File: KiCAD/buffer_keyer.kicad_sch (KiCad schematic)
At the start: 87 parts, among them J1 Conn_01x02_Pin, J13 Conn_01x05, J16 Conn_01x05, T1 2N3906, T2 2N3906, U15 LM7805_TO220, U19 L79L08_TO92, U20 ICL7660S, U3 MC1496, U4 MCP4921, U6 LM7171xIN, U7 LM7171xIN, U8 MCP4728

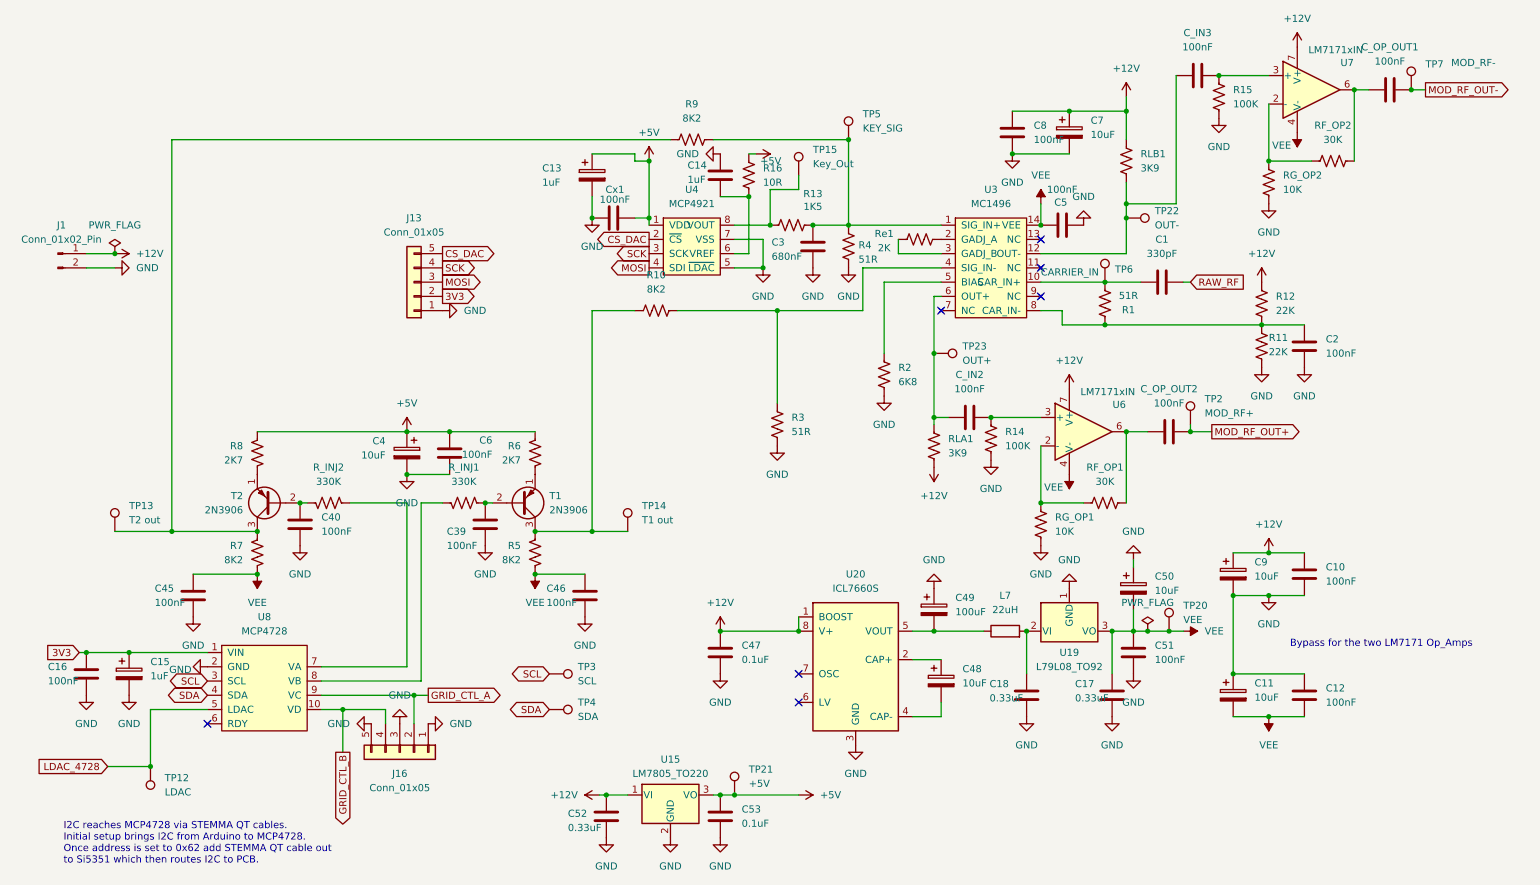
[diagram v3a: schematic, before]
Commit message: kicad: label critical anon nets on buffer_keyer for netclass matching
Global labels on MC1496 out (MC_OUT+/-), LM7171 driver outputs
(DRV_OUT+/-), T1/T2 collectors, and MCP4728 injection nodes
(VA_INJ/VB_INJ). Referenced by RF and HIZ patterns in netclass_patterns.

Co-Authored-By: Claude Opus 4.7 <noreply@anthropic.com>
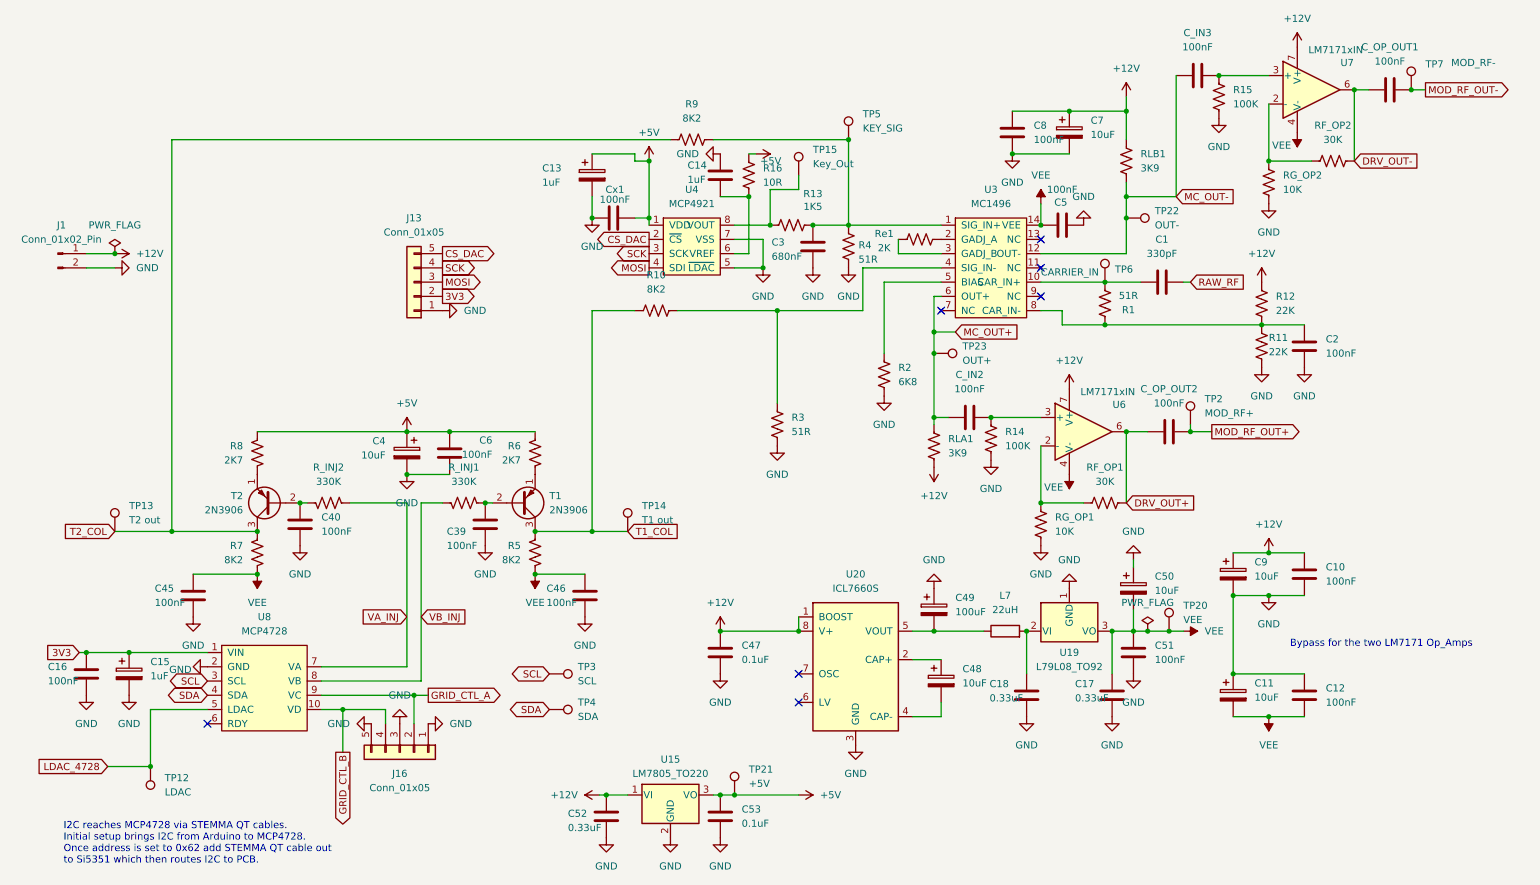
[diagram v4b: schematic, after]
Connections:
- net MC_OUT+: now reaches C_IN2.1, RLA1.2, TP23.1, U3.6 (OUT+)
- net T1_COL: now reaches R10.1, R5.1, T1.3 (C), TP14.1
- net MC_OUT-: now reaches C_IN3.1, RLB1.2, TP22.1, U3.12 (OUT-)
- net T2_COL: now reaches R7.1, R9.1, T2.3 (C), TP13.1
- net VA_INJ: now reaches R_INJ2.1, U8.7 (VA)
- net DRV_OUT-: now reaches C_OP_OUT1.1, RF_OP2.2, U7.6
- net VB_INJ: now reaches R_INJ1.2, U8.8 (VB)
- net DRV_OUT+: now reaches C_OP_OUT2.1, RF_OP1.2, U6.6
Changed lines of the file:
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@@
-	)
-	(junction
-		(at 212.09 52.07)
-		(diameter 0)
-		(color 0 0 0 0)
 	)
 	(junction
@@
 	)
 	(junction
+		(at 177.8 74.93)
+		(diameter 0)
+		(color 0 0 0 0)
+	)
+	(junction
 		(at 237.49 44.45)
 		(diameter 0)
@@
 	(junction
 		(at 142.24 157.48)
+		(diameter 0)
+		(color 0 0 0 0)
+	)
+	(junction
+		(at 212.09 50.8)
 		(diameter 0)
 		(color 0 0 0 0)
@@
 	(wire
 		(pts
-			(xy 212.09 54.61) (xy 212.09 52.07)
+			(xy 212.09 50.8) (xy 212.09 54.61)
 		)
 		(stroke
@@
 	(wire
 		(pts
+			(xy 212.09 50.8) (xy 212.09 48.26)
+		)
+		(stroke
+			(width 0)
+			(type default)
+		)
+	)
+	(wire
+		(pts
 			(xy 177.8 78.74) (xy 177.8 90.17)
 		)
@@
 	(wire
 		(pts
-			(xy 212.09 52.07) (xy 220.98 52.07)
+			(xy 212.09 50.8) (xy 220.98 50.8)
 		)
 		(stroke
@@
 	(wire
 		(pts
+			(xy 181.61 74.93) (xy 177.8 74.93)
+		)
+		(stroke
+			(width 0)
+			(type default)
+		)
+	)
+	(wire
+		(pts
 			(xy 87.63 139.7) (xy 85.09 139.7)
 		)
@@
 	(wire
 		(pts
-			(xy 220.98 52.07) (xy 220.98 29.21)
-		)
-		(stroke
-			(width 0)
-			(type default)
-		)
-	)
-	(wire
-		(pts
-			(xy 212.09 52.07) (xy 212.09 48.26)
+			(xy 220.98 50.8) (xy 220.98 29.21)
 		)
 		(stroke
@@
 	(wire
 		(pts
+			(xy 177.8 74.93) (xy 177.8 78.74)
+		)
+		(stroke
+			(width 0)
+			(type default)
+		)
+	)
+	(wire
+		(pts
 			(xy 231.14 121.92) (xy 237.49 121.92)
 		)
@@
 	(wire
 		(pts
-			(xy 177.8 68.58) (xy 177.8 78.74)
+			(xy 177.8 68.58) (xy 177.8 74.93)
 		)
 		(stroke
@@
 		)
 	)
+	(global_label "VA_INJ"
+		(shape input)
+		(at 83.82 125.73 180)
+		(fields_autoplaced yes)
+		(effects
+			(font
+				(size 1.27 1.27)
+			)
+			(justify right)
+		)
+		(property "Intersheetrefs" "${INTERSHEET_REFS}"
+			(at 74.7871 125.73 0)
+			(hide yes)
+			(show_name no)
+			(do_not_autoplace no)
+			(effects
+				(font
+					(size 1.27 1.27)
+				)
+				(justify right)
+			)
+		)
+	)
 	(global_label "SCL"
 		(shape bidirectional)
@@
 		)
 	)
+	(global_label "MC_OUT+"
+		(shape input)
+		(at 181.61 74.93 0)
+		(fields_autoplaced yes)
+		(effects
+			(font
+				(size 1.27 1.27)
+			)
+			(justify left)
+		)
+		(property "Intersheetrefs" "${INTERSHEET_REFS}"
+			(at 193.4852 74.93 0)
+			(hide yes)
+			(show_name no)
+			(do_not_autoplace no)
+			(effects
+				(font
+					(size 1.27 1.27)
+				)
+				(justify left)
+			)
+		)
+	)
+	(global_label "VB_INJ"
+		(shape input)
+		(at 86.36 125.73 0)
+		(fields_autoplaced yes)
+		(effects
+			(font
+				(size 1.27 1.27)
+			)
+			(justify left)
+		)
+		(property "Intersheetrefs" "${INTERSHEET_REFS}"
+			(at 95.5743 125.73 0)
+			(hide yes)
+			(show_name no)
+			(do_not_autoplace no)
+			(effects
+				(font
+					(size 1.27 1.27)
+				)
+				(justify left)
+			)
+		)
+	)
 	(global_label "SCK"
 		(shape output)
@@
 		)
 	)
+	(global_label "T1_COL"
+		(shape input)
+		(at 123.19 110.49 0)
+		(fields_autoplaced yes)
+		(effects
+			(font
+				(size 1.27 1.27)
+			)
+			(justify left)
+		)
+		(property "Intersheetrefs" "${INTERSHEET_REFS}"
+			(at 132.9485 110.49 0)
+			(hide yes)
+			(show_name no)
+			(do_not_autoplace no)
+			(effects
+				(font
+					(size 1.27 1.27)
+				)
+				(justify left)
+			)
+		)
+	)
 	(global_label "3V3"
 		(shape output)
@@
 		)
 	)
+	(global_label "MC_OUT-"
+		(shape input)
+		(at 220.98 50.8 0)
+		(fields_autoplaced yes)
+		(effects
+			(font
+				(size 1.27 1.27)
+			)
+			(justify left)
+		)
+		(property "Intersheetrefs" "${INTERSHEET_REFS}"
+			(at 232.8552 50.8 0)
+			(hide yes)
+			(show_name no)
+			(do_not_autoplace no)
+			(effects
+				(font
+					(size 1.27 1.27)
+				)
+				(justify left)
+			)
+		)
+	)
+	(global_label "DRV_OUT+"
+		(shape input)
+		(at 212.09 105.41 0)
+		(fields_autoplaced yes)
+		(effects
+			(font
+				(size 1.27 1.27)
+			)
+			(justify left)
+		)
+		(property "Intersheetrefs" "${INTERSHEET_REFS}"
+			(at 224.8724 105.41 0)
+			(hide yes)
+			(show_name no)
+			(do_not_autoplace no)
+			(effects
+				(font
+					(size 1.27 1.27)
+				)
+				(justify left)
+			)
+		)
+	)
 	(global_label "MOSI"
 		(shape output)
@@
 			)
 		)
+	)
+	(global_label "DRV_OUT-"
+		(shape input)
+		(at 252.73 44.45 0)
+		(fields_autoplaced yes)
+		(effects
+			(font
+				(size 1.27 1.27)
+			)
+			(justify left)
+		)
+		(property "Intersheetrefs" "${INTERSHEET_REFS}"
+			(at 265.5124 44.45 0)
+			(hide yes)
+			(show_name no)
+			(do_not_autoplace no)
+			(effects
+				(font
+					(size 1.27 1.27)
+				)
+				(justify left)
+			)
+		)
+	)
+	(global_label "T2_COL"
+		(shape input)
+		(at 31.75 110.49 180)
+		(fields_autoplaced yes)
+		(effects
+			(font
+				(size 1.27 1.27)
+			)
+			(justify right)
+		)
+		(property "Intersheetrefs" "${INTERSHEET_REFS}"
+			(at 21.9915 110.49 0)
+			(hide yes)
+			(show_name no)
+			(do_not_autoplace no)
+			(effects
+				(font
+					(size 1.27 1.27)
+				)
+				(justify right)
+			)
+		)

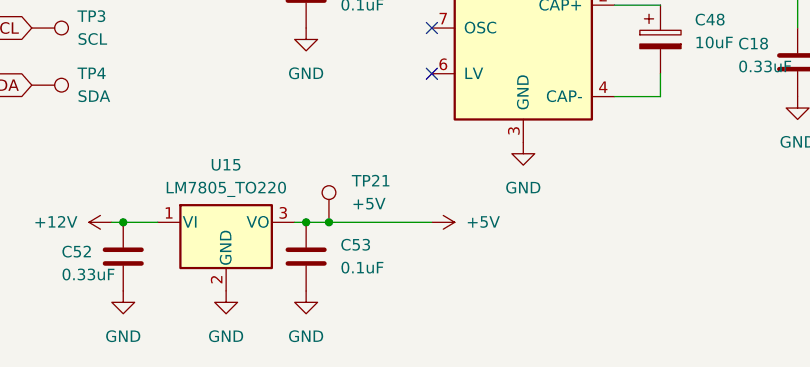
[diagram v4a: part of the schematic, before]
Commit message: kicad: initial routing, netclass tweaks, routing cheatsheet
- Start routing on buffer_keyer PCB (VEE + Net-(U19-VI))
- Netclass assignments and pattern updates for anonymous power nets
  (U19/U20 chain)
- Schematic tweaks alongside routing pass
- Add Documentation/kicad_routing_cheatsheet.md — box-drawing tables
  for shortcut reference readable in `less`

Co-Authored-By: Claude Opus 4.7 <noreply@anthropic.com>
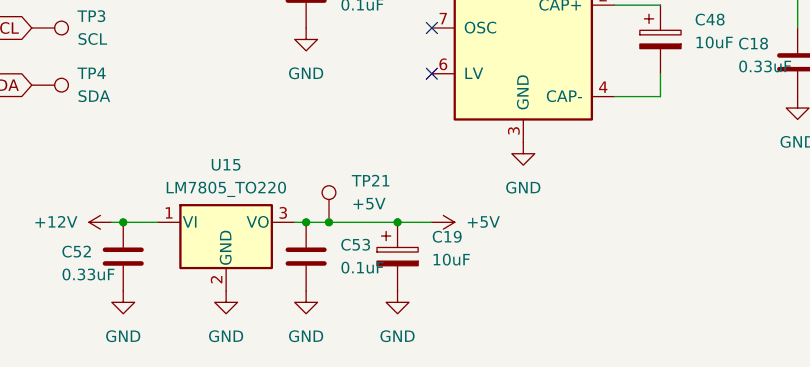
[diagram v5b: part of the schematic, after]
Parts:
- added C19: 10uF, Capacitor_THT:CP_Radial_D5.0mm_P2.00mm, symbol Device:C_Polarized
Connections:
- net +5V: now also C19.1
- net GND: now also C19.2
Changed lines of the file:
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@@
 	)
 	(junction
+		(at 149.86 157.48)
+		(diameter 0)
+		(color 0 0 0 0)
+	)
+	(junction
 		(at 177.8 90.17)
 		(diameter 0)
@@
 	(wire
 		(pts
+			(xy 149.86 157.48) (xy 153.67 157.48)
+		)
+		(stroke
+			(width 0)
+			(type default)
+		)
+	)
+	(wire
+		(pts
 			(xy 252.73 31.75) (xy 255.27 31.75)
 		)
@@
 	(wire
 		(pts
-			(xy 142.24 157.48) (xy 153.67 157.48)
+			(xy 142.24 157.48) (xy 149.86 157.48)
 		)
 		(stroke
@@
 	)
 	(symbol
+		(lib_id "power:GND")
+		(at 149.86 165.1 0)
+		(unit 1)
+		(body_style 1)
+		(exclude_from_sim no)
+		(in_bom yes)
+		(on_board yes)
+		(in_pos_files yes)
+		(dnp no)
+		(fields_autoplaced yes)
+		(property "Reference" "#PWR015"
+			(at 149.86 171.45 0)
+			(hide yes)
+			(show_name no)
+			(do_not_autoplace no)
+			(effects
+				(font
+					(size 1.27 1.27)
+				)
+			)
+		)
+		(property "Value" "GND"
+			(at 149.86 170.18 0)
+			(show_name no)
+			(do_not_autoplace no)
+			(effects
+				(font
+					(size 1.27 1.27)
+				)
+			)
+		)
+		(property "Footprint" ""
+			(at 149.86 165.1 0)
+			(hide yes)
+			(show_name no)
+			(do_not_autoplace no)
+			(effects
+				(font
+					(size 1.27 1.27)
+				)
+			)
+		)
+		(property "Datasheet" ""
+			(at 149.86 165.1 0)
+			(hide yes)
+			(show_name no)
+			(do_not_autoplace no)
+			(effects
+				(font
+					(size 1.27 1.27)
+				)
+			)
+		)
+		(property "Description" "Power symbol creates a global label with name \"GND\" , ground"
+			(at 149.86 165.1 0)
+			(hide yes)
+			(show_name no)
+			(do_not_autoplace no)
+			(effects
+				(font
+					(size 1.27 1.27)
+				)
+			)
+		)
+		(pin "1"
+		)
+		(instances
+			(project "KiCAD"
+				(path "/d3de40b8-856b-4fbd-829c-f45ffcd55742/9b3a5939-c591-4389-8331-709ea54f36b7"
+					(reference "#PWR015")
+					(unit 1)
+				)
+			)
+		)
+	)
+	(symbol
 		(lib_id "Device:C")
 		(at 194.31 139.7 0)
@@
 					(unit 1)
 				)
+			)
+		)
+	)
+	(symbol
+		(lib_id "Device:C_Polarized")
+		(at 149.86 161.29 0)
+		(unit 1)
+		(body_style 1)
+		(exclude_from_sim no)
+		(in_bom yes)
+		(on_board yes)
+		(in_pos_files yes)
+		(dnp no)
+		(fields_autoplaced yes)
+		(property "Reference" "C19"
+			(at 153.67 159.1309 0)
+			(show_name no)
+			(do_not_autoplace no)
+			(effects
+				(font
+					(size 1.27 1.27)
+				)
+				(justify left)
+			)
+		)
+		(property "Value" "10uF"
+			(at 153.67 161.6709 0)
+			(show_name no)
+			(do_not_autoplace no)
+			(effects
+				(font
+					(size 1.27 1.27)
+				)
+				(justify left)
+			)
+		)
+		(property "Footprint" "Capacitor_THT:CP_Radial_D5.0mm_P2.00mm"
+			(at 150.8252 165.1 0)
+			(hide yes)
+			(show_name no)
+			(do_not_autoplace no)
+			(effects
+				(font
+					(size 1.27 1.27)
+				)
+			)
+		)
+		(property "Datasheet" ""
+			(at 149.86 161.29 0)
+			(hide yes)
+			(show_name no)
+			(do_not_autoplace no)
+			(effects
+				(font
+					(size 1.27 1.27)
+				)
+			)
+		)
+		(property "Description" "Polarized capacitor"
+			(at 149.86 161.29 0)
+			(hide yes)
+			(show_name no)
+			(do_not_autoplace no)
+			(effects
+				(font
+					(size 1.27 1.27)
+				)
+			)
+		)
+		(pin "2"
+		)
+		(pin "1"
+		)
+		(instances
+			(project "KiCAD"
+				(path "/d3de40b8-856b-4fbd-829c-f45ffcd55742/9b3a5939-c591-4389-8331-709ea54f36b7"
+					(reference "C19")
+					(unit 1)
+				)

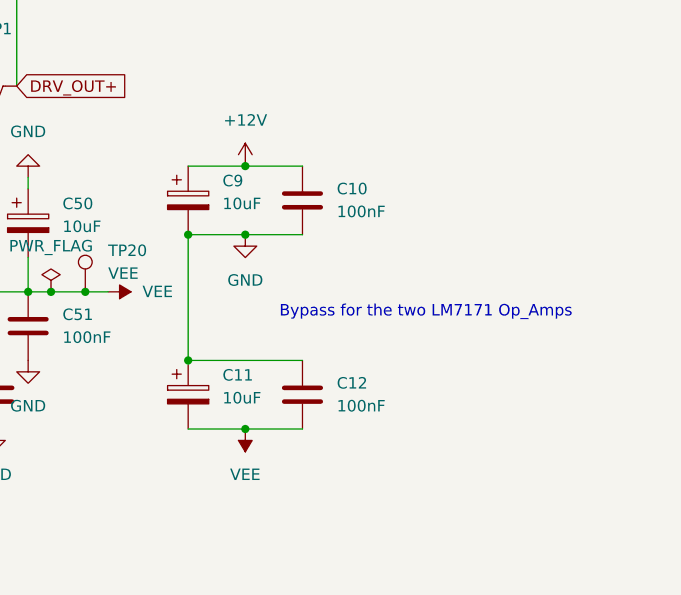
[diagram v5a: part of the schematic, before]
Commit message: kicad: fix GND zone net (was +12V); more routing progress
- Both GND zones on F.Cu and B.Cu had (net "+12V") in the zone
  definition, so pour was filling the wrong net and every GND pad
  showed as unconnected. Corrected to (net "GND").
- Additional routing and placement adjustments on buffer_keyer

Co-Authored-By: Claude Opus 4.7 <noreply@anthropic.com>
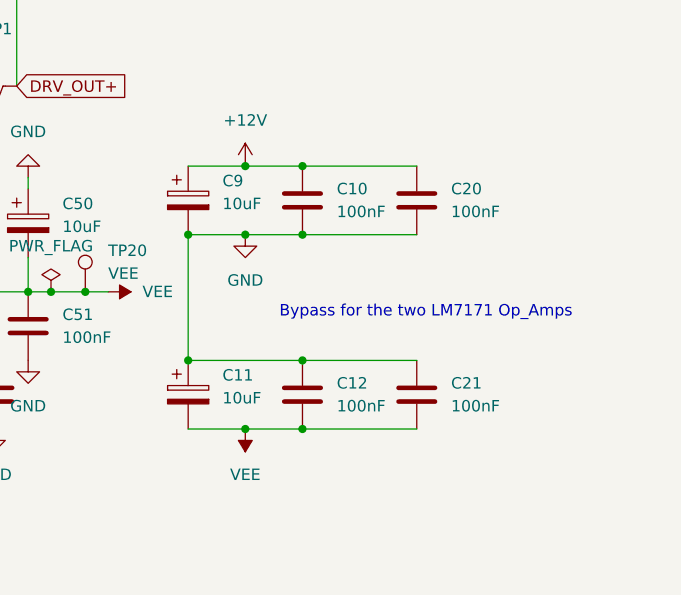
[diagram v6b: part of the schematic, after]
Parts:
- added C20, C21: 100nF, Capacitor_THT:C_Disc_D5.0mm_W2.5mm_P5.00mm, symbol Device:C
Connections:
- net +12V: now also C20.1
- net GND: now also C20.2, C21.1
- net VEE: now also C21.2
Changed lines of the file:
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@@
 	)
 	(junction
+		(at 243.84 114.3)
+		(diameter 0)
+		(color 0 0 0 0)
+	)
+	(junction
 		(at 177.8 90.17)
 		(diameter 0)
@@
 	)
 	(junction
+		(at 243.84 121.92)
+		(diameter 0)
+		(color 0 0 0 0)
+	)
+	(junction
 		(at 212.09 35.56)
 		(diameter 0)
@@
 	)
 	(junction
+		(at 243.84 143.51)
+		(diameter 0)
+		(color 0 0 0 0)
+	)
+	(junction
 		(at 64.77 105.41)
 		(diameter 0)
@@
 	)
 	(junction
+		(at 243.84 135.89)
+		(diameter 0)
+		(color 0 0 0 0)
+	)
+	(junction
 		(at 91.44 92.71)
 		(diameter 0)
@@
 	(wire
 		(pts
+			(xy 243.84 143.51) (xy 256.54 143.51)
+		)
+		(stroke
+			(width 0)
+			(type default)
+		)
+	)
+	(wire
+		(pts
 			(xy 97.79 105.41) (xy 99.06 105.41)
 		)
@@
 	(wire
 		(pts
+			(xy 243.84 135.89) (xy 256.54 135.89)
+		)
+		(stroke
+			(width 0)
+			(type default)
+		)
+	)
+	(wire
+		(pts
 			(xy 236.22 73.66) (xy 243.84 73.66)
 		)
@@
 	(wire
 		(pts
+			(xy 256.54 114.3) (xy 243.84 114.3)
+		)
+		(stroke
+			(width 0)
+			(type default)
+		)
+	)
+	(wire
+		(pts
 			(xy 173.99 128.27) (xy 177.8 128.27)
 		)
@@
 	(wire
 		(pts
+			(xy 243.84 121.92) (xy 256.54 121.92)
+		)
+		(stroke
+			(width 0)
+			(type default)
+		)
+	)
+	(wire
+		(pts
 			(xy 231.14 121.92) (xy 231.14 135.89)
 		)
@@
 	(symbol
 		(lib_id "Device:C")
+		(at 256.54 118.11 0)
+		(unit 1)
+		(body_style 1)
+		(exclude_from_sim no)
+		(in_bom yes)
+		(on_board yes)
+		(in_pos_files yes)
+		(dnp no)
+		(fields_autoplaced yes)
+		(property "Reference" "C20"
+			(at 260.35 116.8399 0)
+			(show_name no)
+			(do_not_autoplace no)
+			(effects
+				(font
+					(size 1.27 1.27)
+				)
+				(justify left)
+			)
+		)
+		(property "Value" "100nF"
+			(at 260.35 119.3799 0)
+			(show_name no)
+			(do_not_autoplace no)
+			(effects
+				(font
+					(size 1.27 1.27)
+				)
+				(justify left)
+			)
+		)
+		(property "Footprint" "Capacitor_THT:C_Disc_D5.0mm_W2.5mm_P5.00mm"
+			(at 257.5052 121.92 0)
+			(hide yes)
+			(show_name no)
+			(do_not_autoplace no)
+			(effects
+				(font
+					(size 1.27 1.27)
+				)
+			)
+		)
+		(property "Datasheet" ""
+			(at 256.54 118.11 0)
+			(hide yes)
+			(show_name no)
+			(do_not_autoplace no)
+			(effects
+				(font
+					(size 1.27 1.27)
+				)
+			)
+		)
+		(property "Description" "Unpolarized capacitor"
+			(at 256.54 118.11 0)
+			(hide yes)
+			(show_name no)
+			(do_not_autoplace no)
+			(effects
+				(font
+					(size 1.27 1.27)
+				)
+			)
+		)
+		(pin "2"
+		)
+		(pin "1"
+		)
+		(instances
+			(project "KiCAD"
+				(path "/d3de40b8-856b-4fbd-829c-f45ffcd55742/9b3a5939-c591-4389-8331-709ea54f36b7"
+					(reference "C20")
+					(unit 1)
+				)
+			)
+		)
+	)
+	(symbol
+		(lib_id "Device:C")
 		(at 209.55 139.7 0)
 		(unit 1)
@@
 					(unit 1)
 				)
+			)
+		)
+	)
+	(symbol
+		(lib_id "Device:C")
+		(at 256.54 139.7 0)
+		(unit 1)
+		(body_style 1)
+		(exclude_from_sim no)
+		(in_bom yes)
+		(on_board yes)
+		(in_pos_files yes)
+		(dnp no)
+		(fields_autoplaced yes)
+		(property "Reference" "C21"
+			(at 260.35 138.4299 0)
+			(show_name no)
+			(do_not_autoplace no)
+			(effects
+				(font
+					(size 1.27 1.27)
+				)
+				(justify left)
+			)
+		)
+		(property "Value" "100nF"
+			(at 260.35 140.9699 0)
+			(show_name no)
+			(do_not_autoplace no)
+			(effects
+				(font
+					(size 1.27 1.27)
+				)
+				(justify left)
+			)
+		)
+		(property "Footprint" "Capacitor_THT:C_Disc_D5.0mm_W2.5mm_P5.00mm"
+			(at 257.5052 143.51 0)
+			(hide yes)
+			(show_name no)
+			(do_not_autoplace no)
+			(effects
+				(font
+					(size 1.27 1.27)
+				)
+			)
+		)
+		(property "Datasheet" ""
+			(at 256.54 139.7 0)
+			(hide yes)
+			(show_name no)
+			(do_not_autoplace no)
+			(effects
+				(font
+					(size 1.27 1.27)
+				)
+			)
+		)
+		(property "Description" "Unpolarized capacitor"
+			(at 256.54 139.7 0)
+			(hide yes)
+			(show_name no)
+			(do_not_autoplace no)
+			(effects
+				(font
+					(size 1.27 1.27)
+				)
+			)
+		)
+		(pin "2"
+		)
+		(pin "1"
+		)
+		(instances
+			(project "KiCAD"
+				(path "/d3de40b8-856b-4fbd-829c-f45ffcd55742/9b3a5939-c591-4389-8331-709ea54f36b7"
+					(reference "C21")
+					(unit 1)
+				)
